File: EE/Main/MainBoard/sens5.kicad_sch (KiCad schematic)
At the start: 3 parts, among them J6 Conn_02x13_Odd_Even

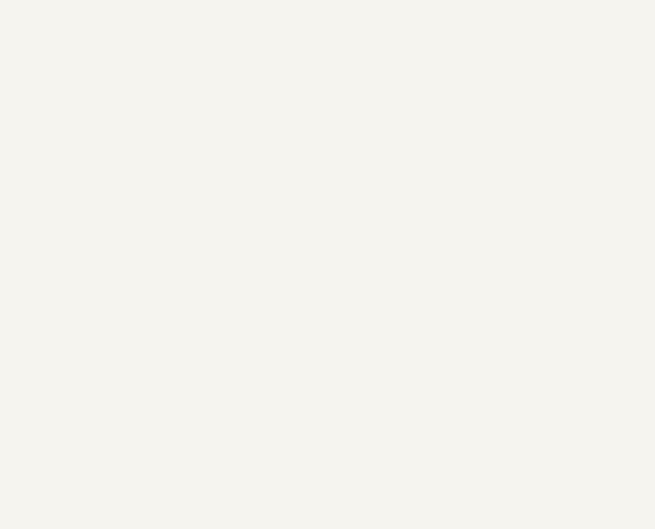
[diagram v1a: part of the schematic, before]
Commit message: WIP - Moving Sensor to IO Expander
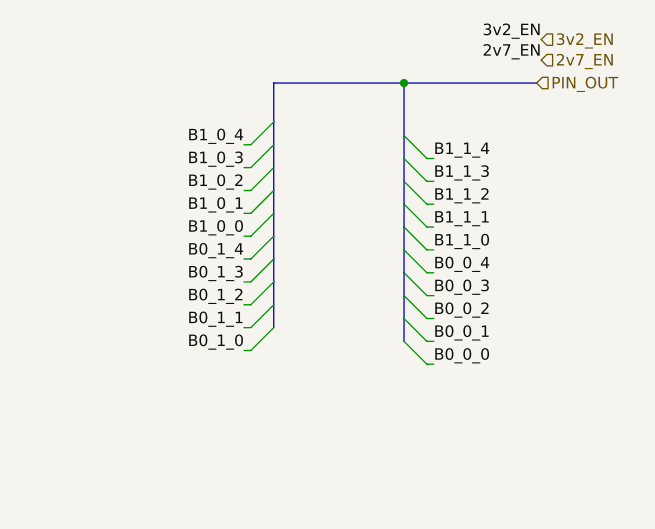
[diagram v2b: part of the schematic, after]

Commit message: Updated layout, and placement for main board
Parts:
- removed J6: Conn_02x13_Odd_Even, Connector_PinHeader_1.27mm:PinHeader_2x13_P1.27mm_Vertical_SMD, symbol Connector_Generic:Conn_02x13_Odd_Even
- added J6: Conn_01x04_Male, Connector_PinSocket_2.54mm:PinSocket_1x04_P2.54mm_Vertical, symbol Connector:Conn_01x04_Male
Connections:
- net GND: now also J6.4 (Pin_4)
- net VCC: now also J6.1 (Pin_1)
- new net SCL: J6.2 (Pin_2)
- new net SDA: J6.3 (Pin_3)
- no-connect marks 2 -> 0

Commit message: Routine Update
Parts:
- H11, H12: footprint MountingHole:MountingHole_2.5mm -> MountingHole:MountingHole_2.7mm
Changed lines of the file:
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@@
       (effects (font (size 1.27 1.27)) (justify left))
     )
-    (property "Footprint" "MountingHole:MountingHole_2.5mm" (id 2) (at 97.282 115.316 0)
+    (property "Footprint" "MountingHole:MountingHole_2.7mm" (id 2) (at 97.282 115.316 0)
       (effects (font (size 1.27 1.27)) hide)
     )
@@
       (effects (font (size 1.27 1.27)) (justify left))
     )
-    (property "Footprint" "MountingHole:MountingHole_2.5mm" (id 2) (at 97.282 71.12 0)
+    (property "Footprint" "MountingHole:MountingHole_2.7mm" (id 2) (at 97.282 71.12 0)
       (effects (font (size 1.27 1.27)) hide)
     )
